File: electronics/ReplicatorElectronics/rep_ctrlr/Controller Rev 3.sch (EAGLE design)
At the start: 80 parts, among them IC2 MICROCHIP_MCP6001-LT, IC3 MICROCHIP_MCP6001-LT, IC4 MICROCHIP_MCP6001-LT, J1 ATX24RH, J10 WASP7PIN, J16 OSTVN04A150, J2 OSTVN04A150, J3 OSTVN04A150, Q1 DISCRETE_MMBT3904LT1G, Q11 DISCRETE_MMBT3904LT1G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

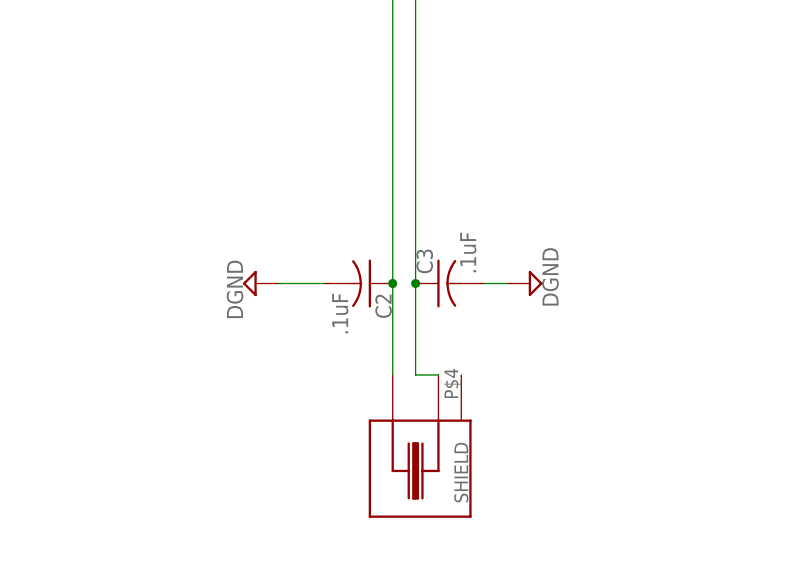
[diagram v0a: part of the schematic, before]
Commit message: Added values for heater section to the overlay
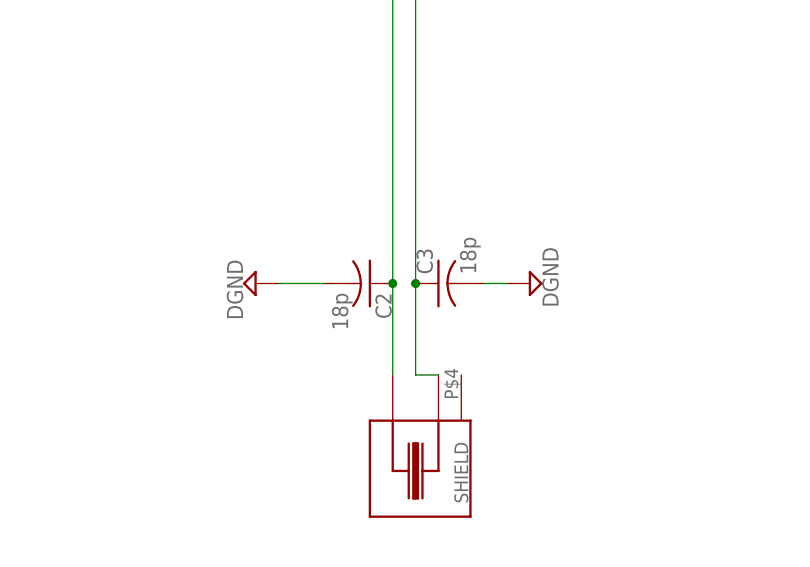
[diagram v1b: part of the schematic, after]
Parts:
- C2, C3: value .1uF -> 18p
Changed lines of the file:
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@@
 <?xml version="1.0" encoding="utf-8"?>
 <!DOCTYPE eagle SYSTEM "eagle.dtd">
-<eagle version="6.5.0">
+<eagle version="6.3">
 <drawing>
 <settings>
@@
 <part name="D1" library="diode" deviceset="CGRM400*-G" device="" technology="7"/>
 <part name="GND13" library="supply2" deviceset="DGND" device=""/>
-<part name="C2" library="rcl" deviceset="C-US" device="C0603" value=".1uF"/>
-<part name="C3" library="rcl" deviceset="C-US" device="C0603" value=".1uF"/>
+<part name="C2" library="rcl" deviceset="C-US" device="C0603" value="18p"/>
+<part name="C3" library="rcl" deviceset="C-US" device="C0603" value="18p"/>
 <part name="R19" library="ResistorBlocks" deviceset="4PACK" device=""/>
 <part name="X2" library="cmr3XXT" deviceset="CMR3XXT" device=""/>
